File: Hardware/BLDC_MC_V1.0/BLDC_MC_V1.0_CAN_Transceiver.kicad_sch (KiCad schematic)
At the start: 14 parts, among them U2 TCAN334DR

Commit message: add the new edits to Buck converter sheet and edit other sheets name
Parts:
- C11: footprint Capacitor_SMD:C_0603_1608Metric -> Capacitor_SMD:C_0805_2012Metric; LCSC_PN C1591 -> C28233; MP CL10B104KB8NNNC -> CL21B104KCFNNNE
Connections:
- net +3.3V: now also C11.1; no longer C11.2
- net GND: now also C11.2; no longer C11.1
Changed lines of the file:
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@@
+	)
+	(symbol
+		(lib_id "Device:C")
+		(at 67.31 87.63 0)
+		(unit 1)
+		(exclude_from_sim no)
+		(in_bom yes)
+		(on_board yes)
+		(dnp no)
+		(fields_autoplaced yes)
+		(property "Reference" "C11"
+			(at 71.12 86.3599 0)
+			(effects
+				(font
+					(size 1.27 1.27)
+				)
+				(justify left)
+			)
+		)
+		(property "Value" "100nF"
+			(at 71.12 88.8999 0)
+			(effects
+				(font
+					(size 1.27 1.27)
+				)
+				(justify left)
+			)
+		)
+		(property "Footprint" "Capacitor_SMD:C_0805_2012Metric"
+			(at 68.2752 91.44 0)
+			(effects
+				(font
+					(size 1.27 1.27)
+				)
+				(hide yes)
+			)
+		)
+		(property "Datasheet" "https://www.lcsc.com/datasheet/C28233.pdf"
+			(at 67.31 87.63 0)
+			(effects
+				(font
+					(size 1.27 1.27)
+				)
+				(hide yes)
+			)
+		)
+		(property "Description" "Unpolarized capacitor"
+			(at 67.31 87.63 0)
+			(effects
+				(font
+					(size 1.27 1.27)
+				)
+				(hide yes)
+			)
+		)
+		(property "LCSC_PN" "C28233"
+			(at 67.31 87.63 0)
+			(effects
+				(font
+					(size 1.27 1.27)
+				)
+				(hide yes)
+			)
+		)
+		(property "MP" "CL21B104KCFNNNE"
+			(at 67.31 87.63 0)
+			(effects
+				(font
+					(size 1.27 1.27)
+				)
+				(hide yes)
+			)
+		)
+		(property "Assembled" "Yes"
+			(at 67.31 87.63 0)
+			(effects
+				(font
+					(size 1.27 1.27)
+				)
+				(hide yes)
+			)
+		)
+		(pin "1"
+		)
+		(pin "2"
+		)
+		(instances
+			(project "BLDC_MC_V1.0"
+				(path "/e34fda66-7244-4ac9-bbf7-3725f03e688f/17c2dea7-3456-4796-810d-fa2277d14545"
+					(reference "C11")
+					(unit 1)
+				)
+			)
+		)
 	)
 	(symbol
@@
 					(unit 1)
 				)
-			)
-		)
-	)
-	(symbol
-		(lib_id "Device:C")
-		(at 67.31 87.63 180)
-		(unit 1)
-		(exclude_from_sim no)
-		(in_bom yes)
-		(on_board yes)
-		(dnp no)
-		(fields_autoplaced yes)
-		(property "Reference" "C11"
-			(at 71.12 86.3599 0)
-			(effects
-				(font
-					(size 1.27 1.27)
-				)
-				(justify right)
-			)
-		)
-		(property "Value" "100nF"
-			(at 71.12 88.8999 0)
-			(effects
-				(font
-					(size 1.27 1.27)
-				)
-				(justify right)
-			)
-		)
-		(property "Footprint" "Capacitor_SMD:C_0603_1608Metric"
-			(at 66.3448 83.82 0)
-			(effects
-				(font
-					(size 1.27 1.27)
-				)
-				(hide yes)
-			)
-		)
-		(property "Datasheet" "https://www.lcsc.com/datasheet/C1591.pdf"
-			(at 67.31 87.63 0)
-			(effects
-				(font
-					(size 1.27 1.27)
-				)
-				(hide yes)
-			)
-		)
-		(property "Description" "Unpolarized capacitor"
-			(at 67.31 87.63 0)
-			(effects
-				(font
-					(size 1.27 1.27)
-				)
-				(hide yes)
-			)
-		)
-		(property "MP" "CL10B104KB8NNNC"
-			(at 67.31 87.63 90)
-			(effects
-				(font
-					(size 1.27 1.27)
-				)
-				(hide yes)
-			)
-		)
-		(property "LCSC_PN" "C1591"
-			(at 67.31 87.63 90)
-			(effects
-				(font
-					(size 1.27 1.27)
-				)
-				(hide yes)
-			)
-		)
-		(property "Assembled" "Yes"
-			(at 67.31 87.63 0)
-			(effects
-				(font
-					(size 1.27 1.27)
-				)
-				(hide yes)
-			)
-		)
-		(pin "1"
-		)
-		(pin "2"
-		)
-		(instances
-			(project "BLDC_Motor_Driver"
-				(path "/e34fda66-7244-4ac9-bbf7-3725f03e688f/17c2dea7-3456-4796-810d-fa2277d14545"
-					(reference "C11")
-					(unit 1)
-				)

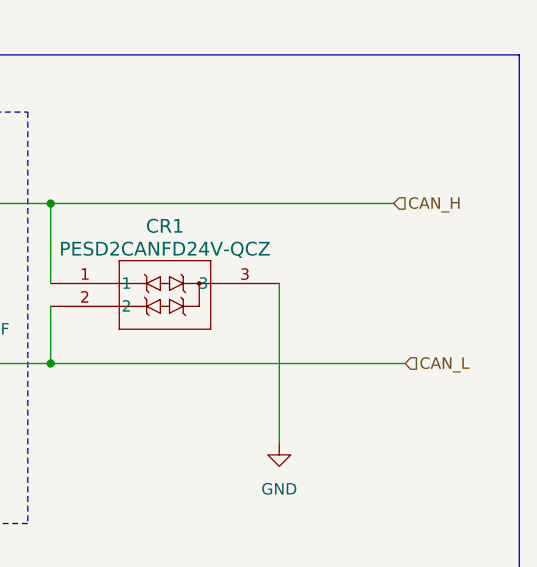
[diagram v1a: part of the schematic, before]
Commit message: Edit the connection between sheets and add some details and connections to gatedrive sheet
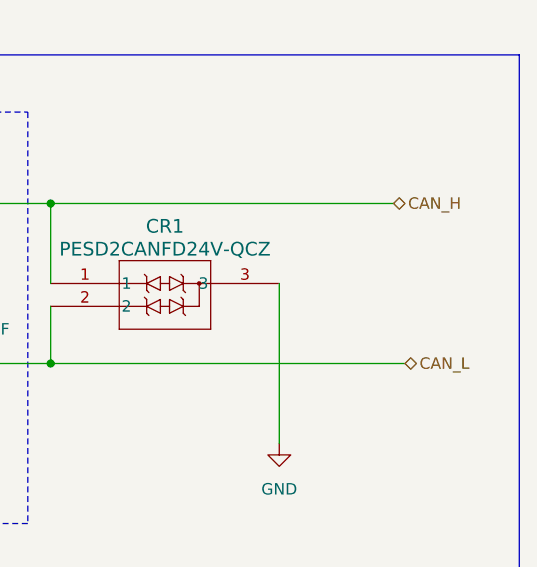
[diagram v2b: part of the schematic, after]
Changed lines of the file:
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@@
 	)
 	(hierarchical_label "CAN_H"
-		(shape input)
+		(shape bidirectional)
 		(at 246.38 77.47 0)
 		(effects
@@
 	)
 	(hierarchical_label "CAN_L"
-		(shape input)
+		(shape bidirectional)
 		(at 247.65 95.25 0)
 		(effects

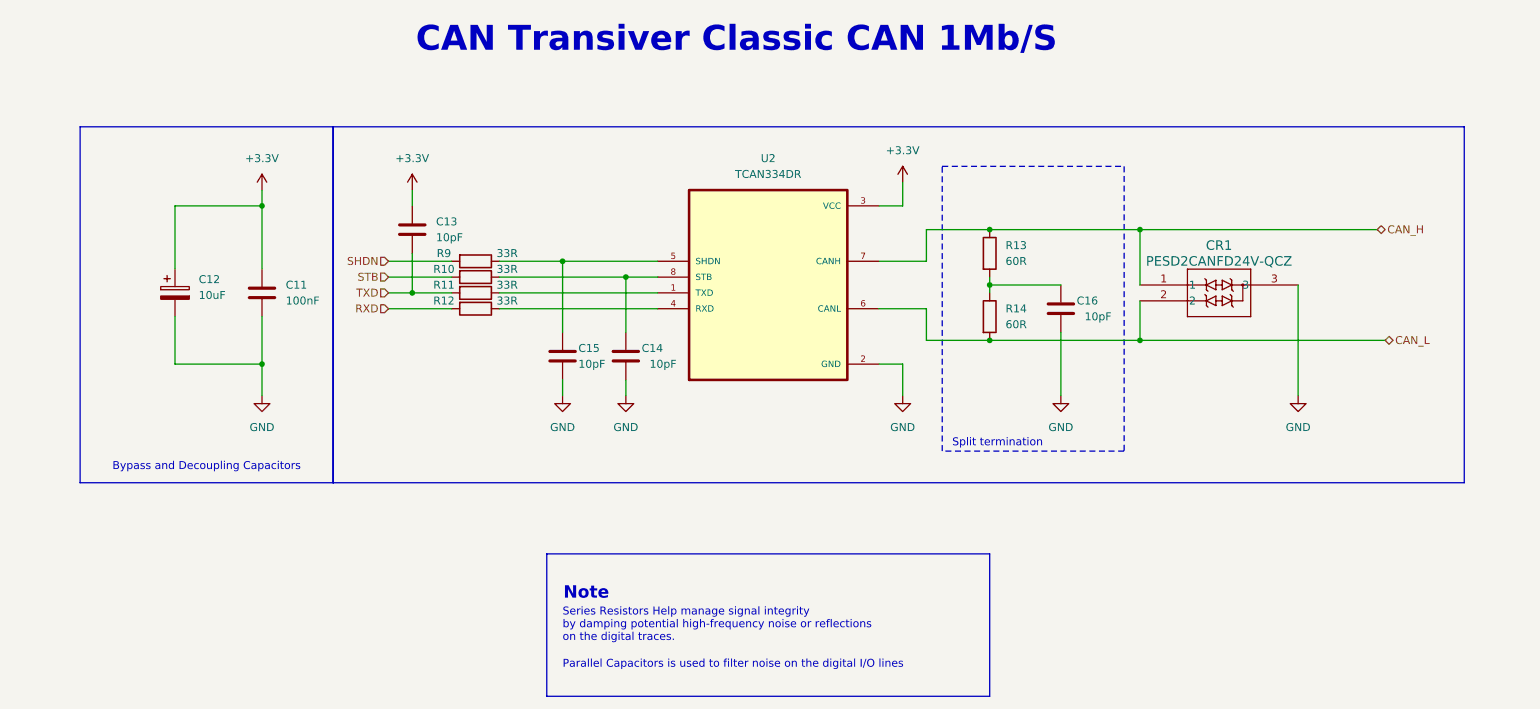
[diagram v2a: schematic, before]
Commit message: Add CAN bus Chake
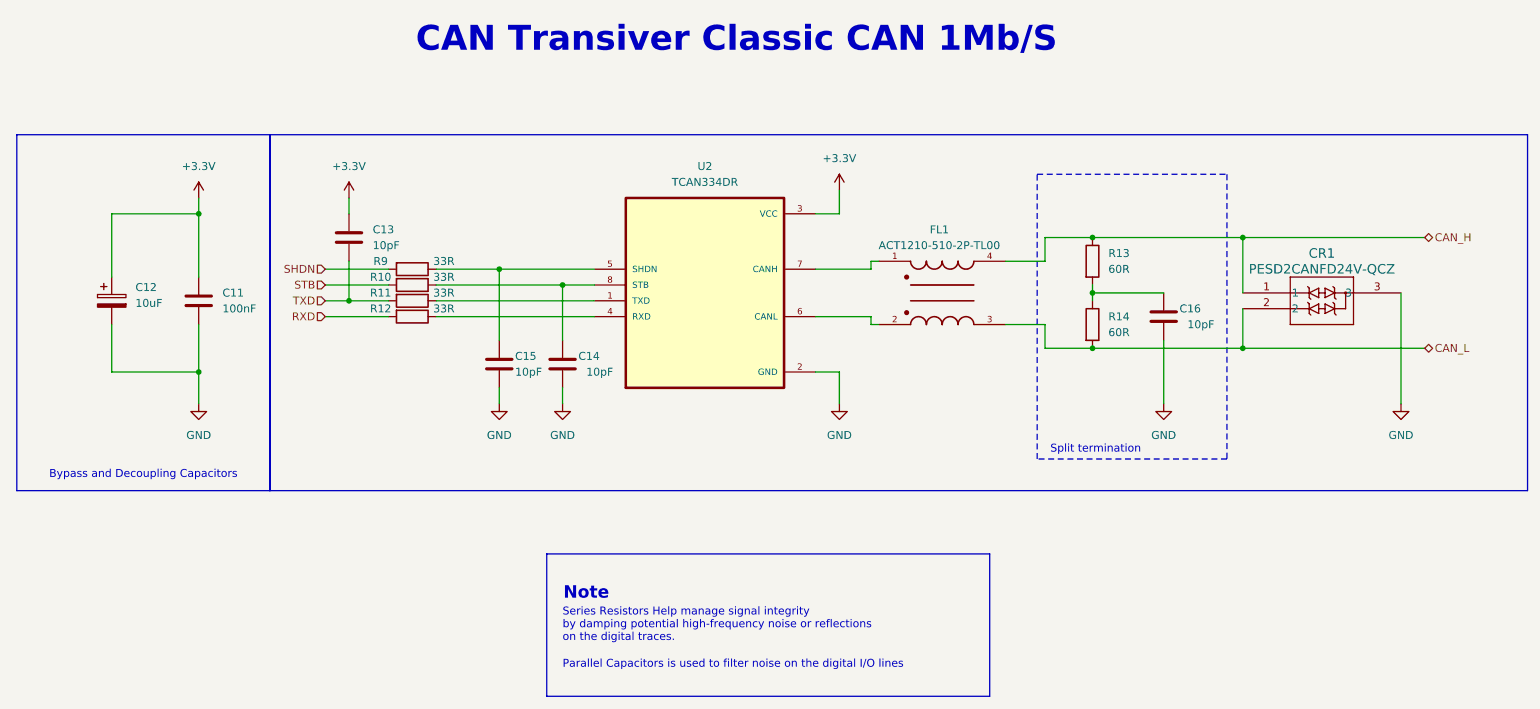
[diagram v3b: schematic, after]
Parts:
- added FL1: ACT1210-510-2P-TL00, BLDC_Motor_Driver_Components_Footprint:FIL_ACT1210-510-2P-TL00, symbol ACT1210-510-2P-TL00:ACT1210-510-2P-TL00
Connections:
- net CAN_H: now also FL1.4; no longer U2.7 (CANH)
- net CAN_L: now also FL1.3; no longer U2.6 (CANL)
- new net: FL1.2, U2.6 (CANL)
- new net: FL1.1, U2.7 (CANH)
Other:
- moved on the sheet: C11, C12, C13, C14, C15, C16, CR1, R10, R11, R12, R13, R14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

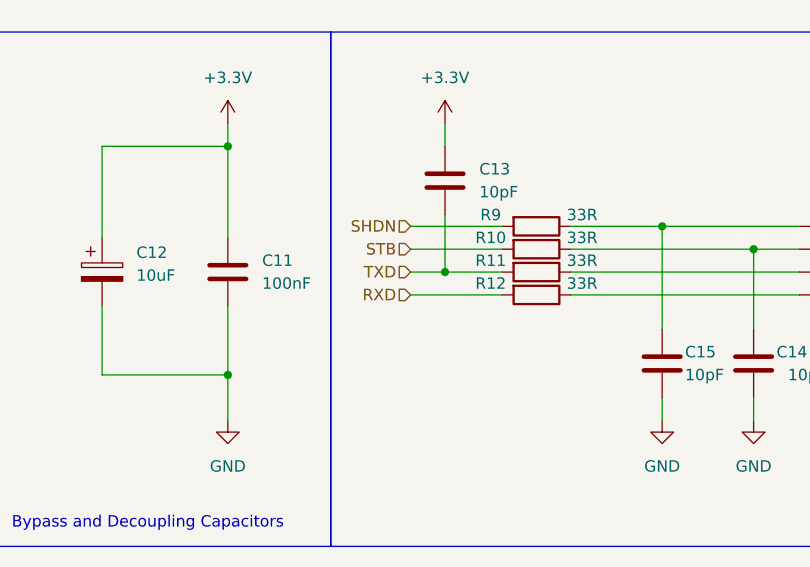
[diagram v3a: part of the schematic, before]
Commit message: Edit Controller sheet and add oscillators for the controller
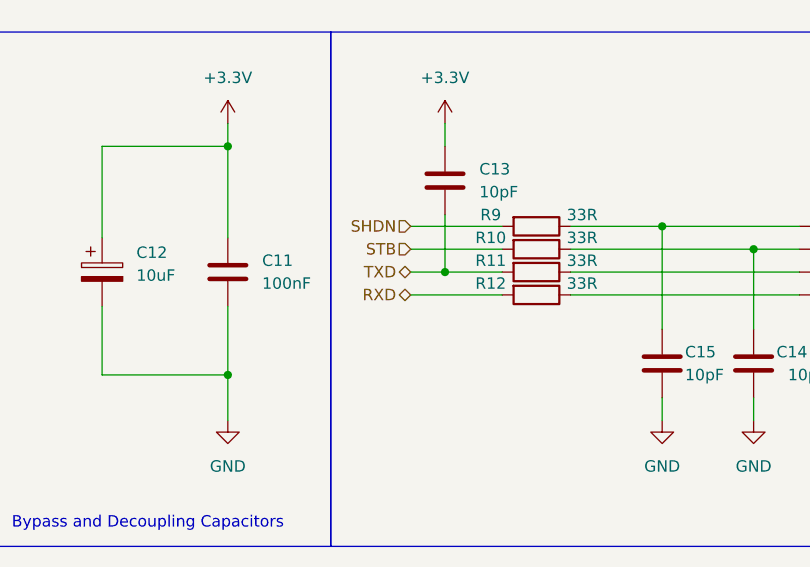
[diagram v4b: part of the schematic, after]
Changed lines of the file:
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@@
 	)
 	(hierarchical_label "RXD"
-		(shape input)
+		(shape bidirectional)
 		(at 77.47 91.44 180)
 		(effects
@@
 	)
 	(hierarchical_label "TXD"
-		(shape input)
+		(shape bidirectional)
 		(at 77.47 88.9 180)
 		(effects

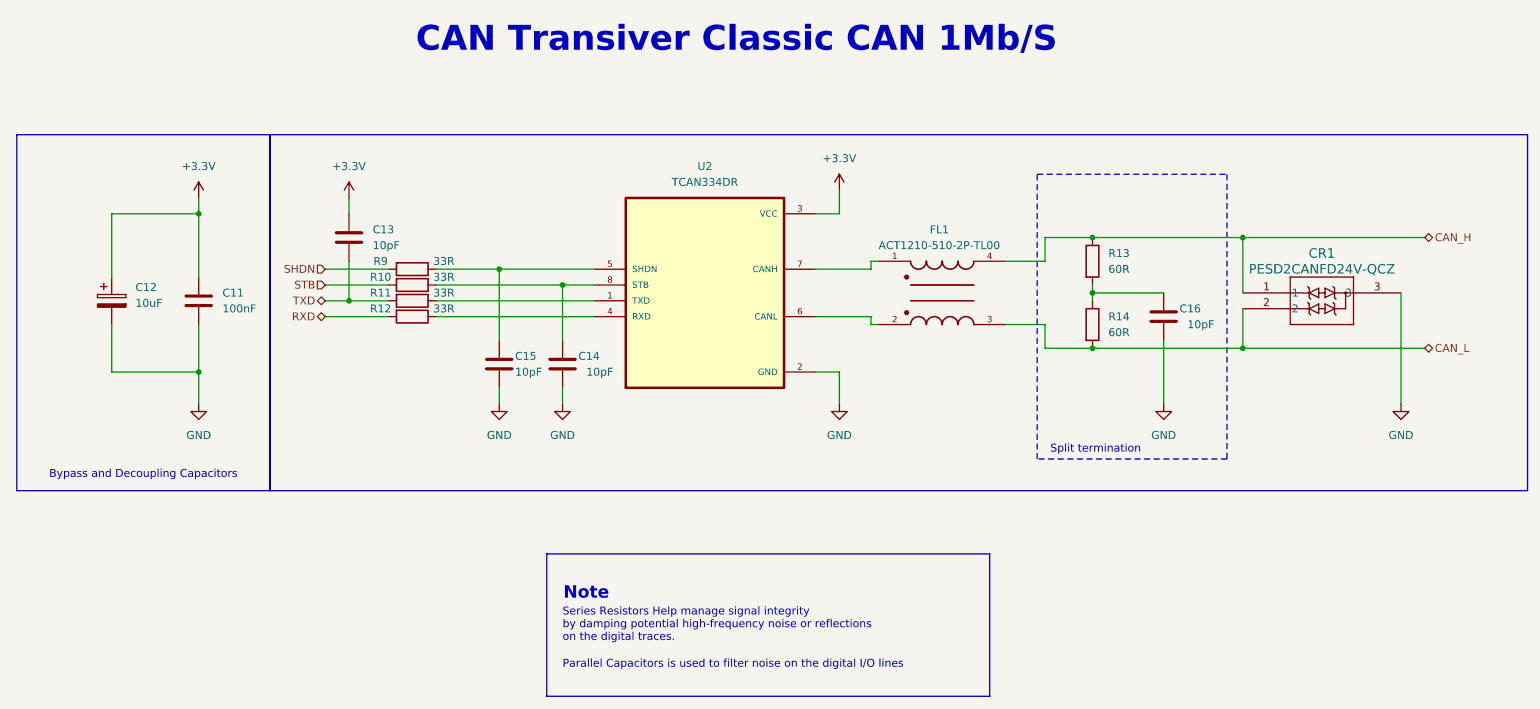
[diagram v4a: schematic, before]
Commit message: Edit the controller sheet and CAN sheet to adjust the interface between them
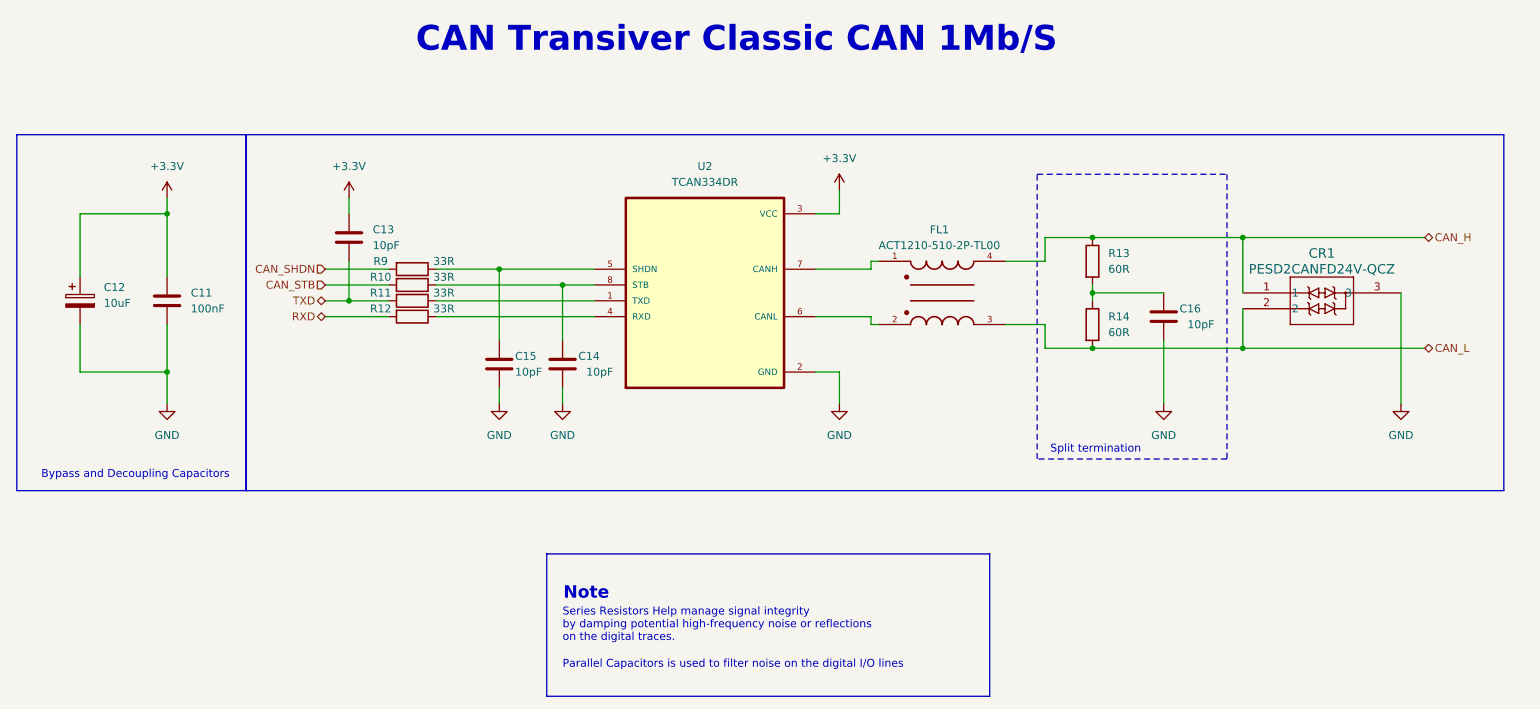
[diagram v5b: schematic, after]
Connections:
- net SHDN renamed CAN_SHDN
- net STB renamed CAN_STB
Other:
- moved on the sheet: C11, C12
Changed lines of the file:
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@@
 	)
 	(rectangle
-		(start 68.58 62.23)
-		(end 270.51 119.38)
+		(start 64.77 62.23)
+		(end 266.7 119.38)
 		(stroke
 			(width 0)
@@
 	(rectangle
 		(start 27.94 62.23)
-		(end 68.58 119.38)
+		(end 64.77 119.38)
 		(stroke
 			(width 0)
@@
 	(text "Bypass and Decoupling Capacitors\n"
 		(exclude_from_sim no)
-		(at 48.26 116.84 0)
+		(at 46.99 116.84 0)
 		(effects
 			(font
@@
 	)
 	(junction
-		(at 57.15 74.93)
+		(at 52.07 74.93)
 		(diameter 0)
 		(color 0 0 0 0)
@@
 	)
 	(junction
-		(at 57.15 100.33)
+		(at 52.07 100.33)
 		(diameter 0)
 		(color 0 0 0 0)
@@
 	(wire
 		(pts
-			(xy 57.15 92.71) (xy 57.15 100.33)
-		)
-		(stroke
-			(width 0)
-			(type default)
-		)
-	)
-	(wire
-		(pts
-			(xy 57.15 100.33) (xy 57.15 105.41)
+			(xy 52.07 92.71) (xy 52.07 100.33)
+		)
+		(stroke
+			(width 0)
+			(type default)
+		)
+	)
+	(wire
+		(pts
+			(xy 52.07 100.33) (xy 52.07 105.41)
 		)
 		(stroke
@@
 	(wire
 		(pts
-			(xy 43.18 85.09) (xy 43.18 74.93)
+			(xy 38.1 85.09) (xy 38.1 74.93)
 		)
 		(stroke
@@
 	(wire
 		(pts
-			(xy 43.18 92.71) (xy 43.18 100.33)
+			(xy 38.1 92.71) (xy 38.1 100.33)
 		)
 		(stroke
@@
 	(wire
 		(pts
-			(xy 57.15 72.39) (xy 57.15 74.93)
+			(xy 52.07 72.39) (xy 52.07 74.93)
 		)
 		(stroke
@@
 	(wire
 		(pts
-			(xy 43.18 74.93) (xy 57.15 74.93)
+			(xy 38.1 74.93) (xy 52.07 74.93)
 		)
 		(stroke
@@
 	(wire
 		(pts
-			(xy 57.15 74.93) (xy 57.15 85.09)
+			(xy 52.07 74.93) (xy 52.07 85.09)
 		)
 		(stroke
@@
 	(wire
 		(pts
-			(xy 43.18 100.33) (xy 57.15 100.33)
+			(xy 38.1 100.33) (xy 52.07 100.33)
 		)
 		(stroke
@@
 		)
 	)
-	(hierarchical_label "STB"
+	(hierarchical_label "CAN_STB"
 		(shape input)
 		(at 77.47 86.36 180)
@@
 		)
 	)
-	(hierarchical_label "SHDN"
+	(hierarchical_label "CAN_SHDN"
 		(shape input)
 		(at 77.47 83.82 180)
@@
 	(symbol
 		(lib_id "power:GND")
-		(at 57.15 105.41 0)
+		(at 52.07 105.41 0)
 		(unit 1)
 		(exclude_from_sim no)
@@
 		(fields_autoplaced yes)
 		(property "Reference" "#PWR023"
-			(at 57.15 111.76 0)
+			(at 52.07 111.76 0)
 			(effects
 				(font
@@
 		)
 		(property "Value" "GND"
-			(at 57.15 110.49 0)
+			(at 52.07 110.49 0)
 			(effects
 				(font
@@
 		)
 		(property "Footprint" ""
-			(at 57.15 105.41 0)
+			(at 52.07 105.41 0)
 			(effects
 				(font
@@
 		)
 		(property "Datasheet" ""
-			(at 57.15 105.41 0)
+			(at 52.07 105.41 0)
 			(effects
 				(font
@@
 		)
 		(property "Description" "Power symbol creates a global label with name \"GND\" , ground"
-			(at 57.15 105.41 0)
+			(at 52.07 105.41 0)
 			(effects
 				(font
@@
 	(symbol
 		(lib_id "Device:C_Polarized")
-		(at 43.18 88.9 0)
+		(at 38.1 88.9 0)
 		(unit 1)
 		(exclude_from_sim no)
@@
 		(fields_autoplaced yes)
 		(property "Reference" "C12"
-			(at 46.99 86.7409 0)
+			(at 41.91 86.7409 0)
 			(effects
 				(font
@@
 		)
 		(property "Value" "10uF"
-			(at 46.99 89.2809 0)
+			(at 41.91 89.2809 0)
 			(effects
 				(font
@@
 		)
 		(property "Footprint" "Capacitor_Tantalum_SMD:CP_EIA-3216-18_Kemet-A"
-			(at 44.1452 92.71 0)
+			(at 39.0652 92.71 0)
 			(effects
 				(font
@@
 		)
 		(property "Datasheet" "https://datasheets.kyocera-avx.com/TAJ.pdf"
-			(at 43.18 88.9 0)
+			(at 38.1 88.9 0)
 			(effects
 				(font
@@
 		)
 		(property "Description" "Polarized capacitor"
-			(at 43.18 88.9 0)
+			(at 38.1 88.9 0)
 			(effects
 				(font
@@
 		)
 		(property "LCSC_PN" "C7171"
-			(at 43.18 88.9 0)
+			(at 38.1 88.9 0)
 			(effects
 				(font
@@
 		)
 		(property "MP" "TAJA106K016RNJ"
-			(at 43.18 88.9 0)
+			(at 38.1 88.9 0)
 			(effects
 				(font
@@
 		)
 		(property "Assembled" "Yes"
-			(at 43.18 88.9 0)
+			(at 38.1 88.9 0)
 			(effects
 				(font
@@
 	(symbol
 		(lib_id "power:+3.3V")
-		(at 57.15 72.39 0)
+		(at 52.07 72.39 0)
 		(unit 1)
 		(exclude_from_sim no)
@@
 		(fields_autoplaced yes)
 		(property "Reference" "#PWR022"
-			(at 57.15 76.2 0)
+			(at 52.07 76.2 0)
 			(effects
 				(font
@@
 		)
 		(property "Value" "+3.3V"
-			(at 57.15 67.31 0)
+			(at 52.07 67.31 0)
 			(effects
 				(font
@@
 		)
 		(property "Footprint" ""
-			(at 57.15 72.39 0)
+			(at 52.07 72.39 0)
 			(effects
 				(font
@@
 		)
 		(property "Datasheet" ""
-			(at 57.15 72.39 0)
+			(at 52.07 72.39 0)
 			(effects
 				(font
@@
 		)
 		(property "Description" "Power symbol creates a global label with name \"+3.3V\""
-			(at 57.15 72.39 0)
+			(at 52.07 72.39 0)
 			(effects
 				(font
@@
 	(symbol
 		(lib_id "Device:C")
-		(at 57.15 88.9 0)
+		(at 52.07 88.9 0)
 		(unit 1)
 		(exclude_from_sim no)
@@
 		(fields_autoplaced yes)
 		(property "Reference" "C11"
-			(at 60.96 87.6299 0)
+			(at 55.88 87.6299 0)
 			(effects
 				(font
@@
 		)
 		(property "Value" "100nF"
-			(at 60.96 90.1699 0)
+			(at 55.88 90.1699 0)
 			(effects
 				(font
@@
 		)
 		(property "Footprint" "Capacitor_SMD:C_0805_2012Metric"
-			(at 58.1152 92.71 0)
+			(at 53.0352 92.71 0)
 			(effects
 				(font
@@
 		)
 		(property "Datasheet" "https://www.lcsc.com/datasheet/C28233.pdf"
-			(at 57.15 88.9 0)
+			(at 52.07 88.9 0)
 			(effects
 				(font
@@
 		)
 		(property "Description" "Unpolarized capacitor"
-			(at 57.15 88.9 0)
+			(at 52.07 88.9 0)
 			(effects
 				(font
@@
 		)
 		(property "LCSC_PN" "C28233"
-			(at 57.15 88.9 0)
+			(at 52.07 88.9 0)
 			(effects
 				(font
@@
 		)
 		(property "MP" "CL21B104KCFNNNE"
-			(at 57.15 88.9 0)
+			(at 52.07 88.9 0)
 			(effects
 				(font
@@
 		)
 		(property "Assembled" "Yes"
-			(at 57.15 88.9 0)
-			(effects
-				(font
+			(at 52.07 88.9 0)
+			(effects
+				(font
